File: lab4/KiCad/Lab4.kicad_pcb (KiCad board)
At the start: 2 copper layers, 120 x 234 mm, 287 parts, among them J1 Sense test points, J10 CAN A isolation, J11 CAN A test, J14 CAN B isolation, J15 CAN B test, J2 Current test, J20 CAN A isolation, J21 CAN A test, J24 CAN B isolation, J25 CAN B test, J3 Current test, J30 CAN A isolation, J31 CAN A test, J34 CAN B isolation, J35 CAN B test, J40 Battery input: 1=+ 2=GND, J41 VBAT test, J42 Rail / PG / GND, J43 Rail / PG / GND, J44 Rail / PG / GND, J500 BOOT recovery, J501 SWD (2.54mm), J502 3.3V TTL UART, J503 LAB3 rows 1-13, J504 Additional probes, J505 Reserved / encoder probes, J550 FRONT LEFT lamp, J551 FRONT RIGHT lamp, J600 BOOT recovery, J601 SWD (2.54mm), J602 3.3V TTL UART, J603 LAB3 rows 1-13, J604 Additional probes, J605 Reserved / encoder probes, J650 REAR LEFT lamp, J651 REAR RIGHT lamp, J70 Raspberry Pi4 GPIO, J703 LAB3 rows 1-13, J704 Pi extra probes, J80 LEFT motor, J81 RIGHT motor, J82 LEFT encoder, J83 RIGHT encoder, J90 Servo: GND / 6.6V / PWM, Q1 DMPH3010LK3-13, Q550 MMBT3904, Q551 MMBT3904, Q650 MMBT3904, Q651 MMBT3904, U1 INA180A2IDBVR, U10 MCP2515T-I/ST, U11 SN65HVD231DR, U14 MCP2515T-I/ST, U15 SN65HVD231DR, U2 ACS712ELCTR-05B-T, U20 MCP2515T-I/ST, U21 SN65HVD231DR, U24 MCP2515T-I/ST, U25 SN65HVD231DR, U3 ACS712ELCTR-05B-T, U30 MCP2515T-I/ST, U31 SN65HVD231DR, U34 MCP2515T-I/ST, U35 SN65HVD231DR, U40 TPS564252DRLR, U41 TPS564252DRLR, U42 TPS564252DRLR, U50 STM32F401RET6TR, U60 STM32F401RET6TR, U80 L298N, U81 SN74LVC14APWR, Y10 16 MHz, Y14 16 MHz, Y20 16 MHz, Y24 16 MHz, Y30 16 MHz, Y34 16 MHz

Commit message: Add verified GCT switch footprints and refresh Lab 4 checks
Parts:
- added SW50: SWT0210-045026GSA, Lab4_Switches:GCT_SWT0210_4.5x4.5mm, F.Cu at (52.0, 225.0)
- added SW51: SWT0210-045026GSA, Lab4_Switches:GCT_SWT0210_4.5x4.5mm, F.Cu at (100.0, 219.0)
- added SW60: SWT0210-045026GSA, Lab4_Switches:GCT_SWT0210_4.5x4.5mm, F.Cu at (52.0, 121.0)
- added SW61: SWT0210-045026GSA, Lab4_Switches:GCT_SWT0210_4.5x4.5mm, F.Cu at (67.0, 125.0)
- added SW70: SWT0210-045026GSA, Lab4_Switches:GCT_SWT0210_4.5x4.5mm, F.Cu at (52.0, 184.0)
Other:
- board text removed: "SW50 RESET"
- board text removed: "SW51 SELF TEST"
- board text removed: "SW60 RESET"
- board text removed: "SW61 SELF TEST"
- board text removed: "SW70 PI TEST"

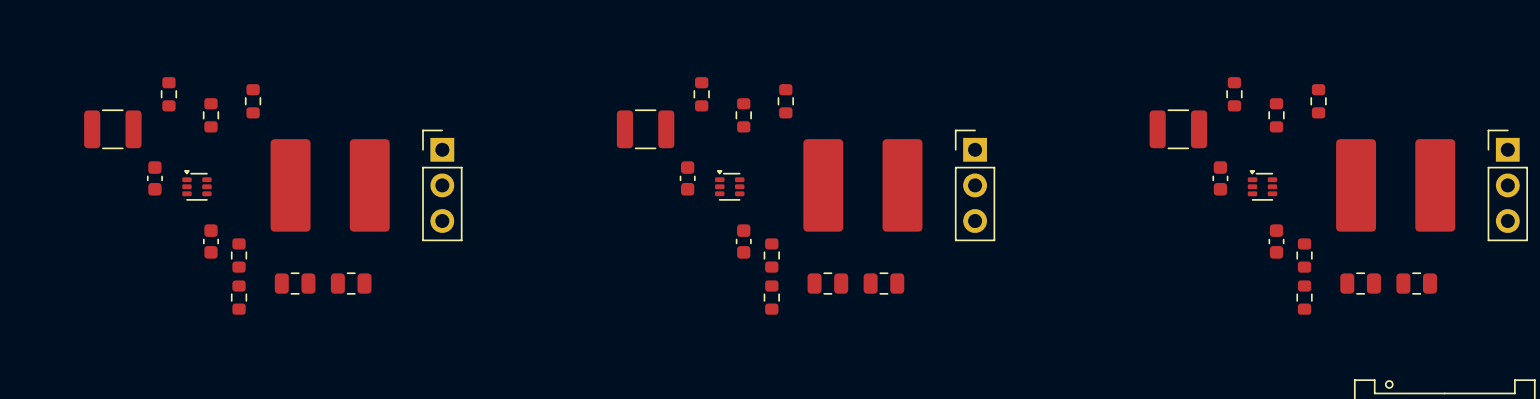
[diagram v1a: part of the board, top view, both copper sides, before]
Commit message: Refine regulator placement and verify buck support circuits
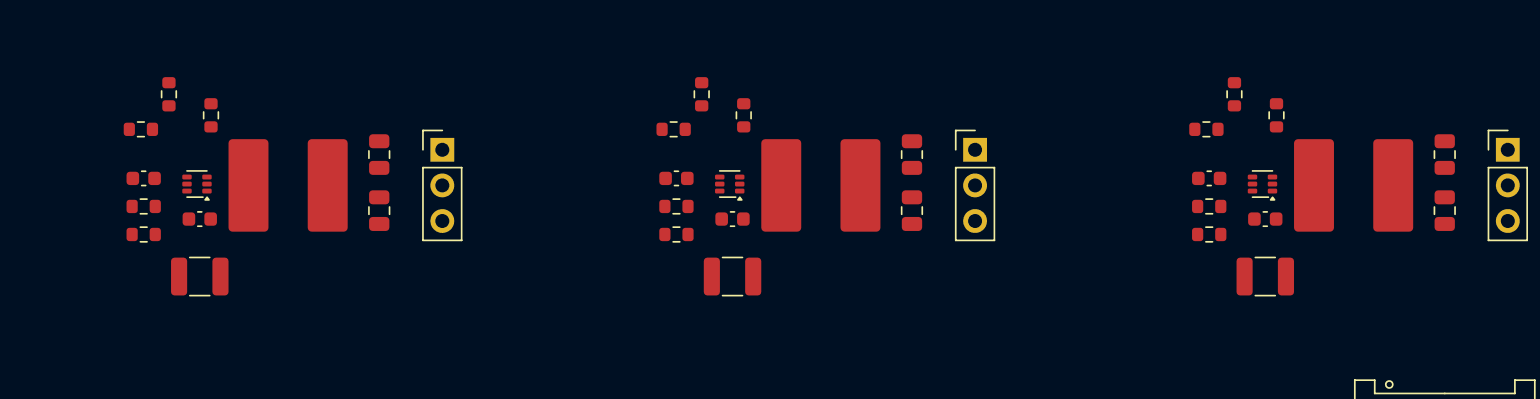
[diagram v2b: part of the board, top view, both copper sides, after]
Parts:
- moved C410 12.2 mm to (58.2, 250.5), turned to 180 degrees
- moved C420 12.2 mm to (96.2, 250.5), turned to 180 degrees
- moved C430 12.2 mm to (134.2, 250.5), turned to 180 degrees
- moved C412 11.0 mm to (71.0, 241.8), turned to 90 degrees
- moved C422 11.0 mm to (109.0, 241.8), turned to 90 degrees
- moved C432 11.0 mm to (147.0, 241.8), turned to 90 degrees
- moved R414 8.25 mm to (54.0, 240.0), turned to 0 degrees
- moved R424 8.25 mm to (92.0, 240.0), turned to 0 degrees
- moved R434 8.25 mm to (130.0, 240.0), turned to 0 degrees
- moved R431 8.15 mm to (130.2, 247.5), turned to 180 degrees
- moved R411 8.15 mm to (54.2, 247.5), turned to 180 degrees
- moved R421 8.15 mm to (92.2, 247.5), turned to 180 degrees
- moved R430 7.65 mm to (130.2, 245.5), turned to 0 degrees
- moved R410 7.65 mm to (54.2, 245.5), turned to 0 degrees
- moved R420 7.65 mm to (92.2, 245.5), turned to 0 degrees
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
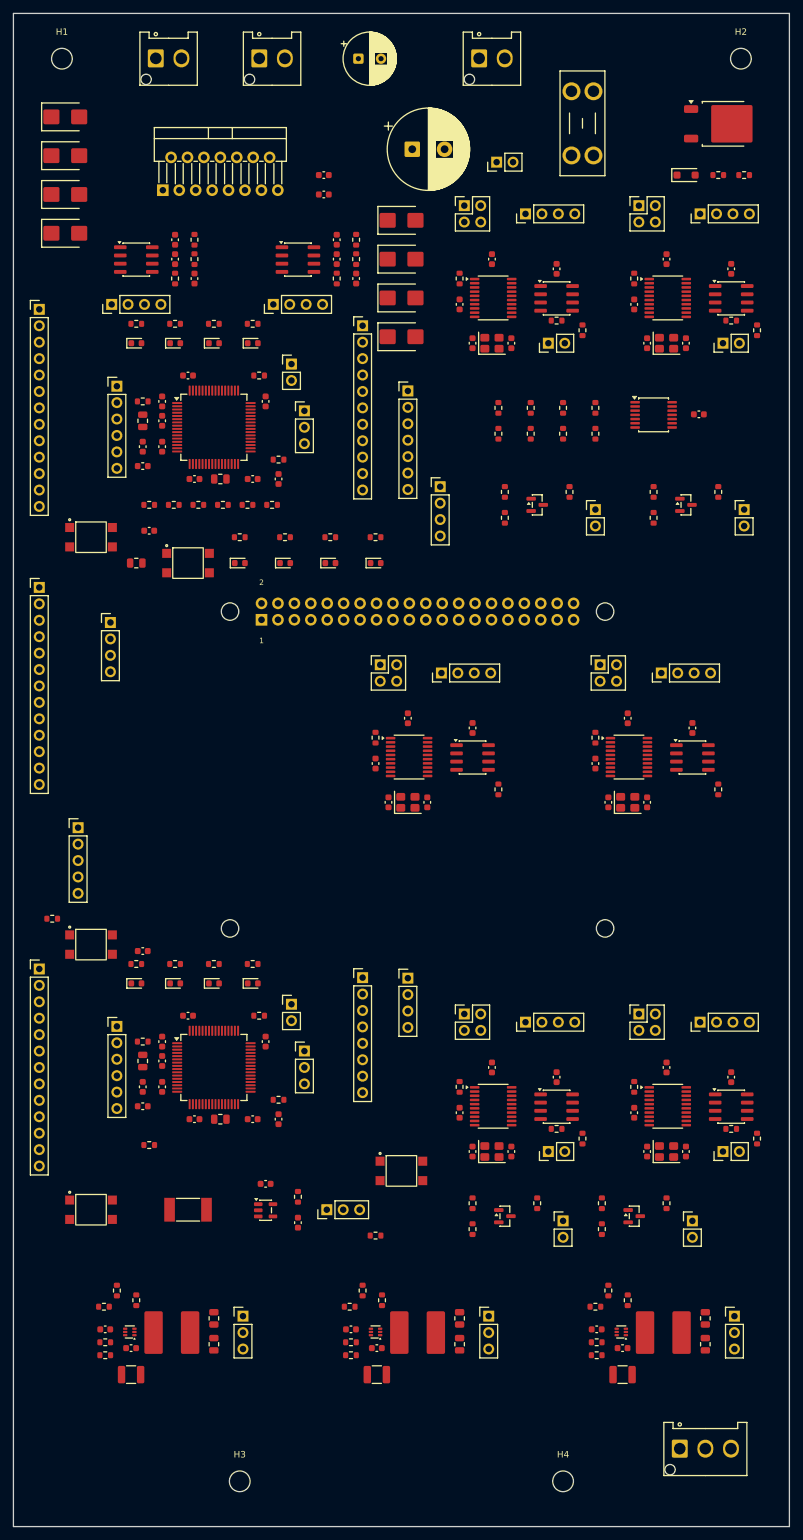
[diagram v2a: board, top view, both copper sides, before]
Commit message: Start regulator copper routing and verify local connectivity
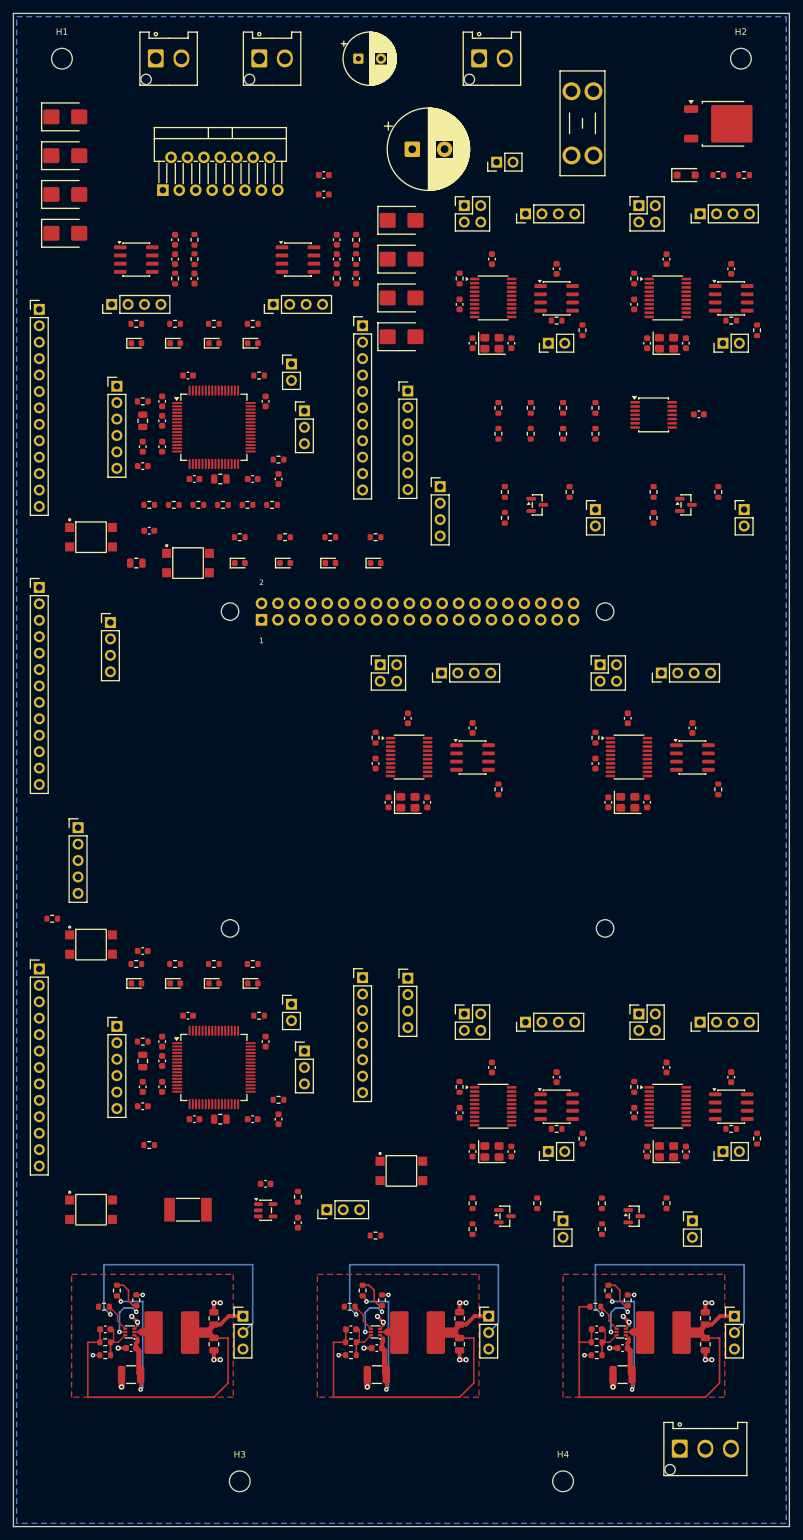
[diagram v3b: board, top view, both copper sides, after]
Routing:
- net /VBAT_PROTECTED: track 0.00 -> 81.7 mm, vias 0 -> 6
- net /+3V3: track 0.00 -> 61.9 mm
- net /+6V6_SERVO: track 0.00 -> 54.8 mm
- net /+5V: track 0.00 -> 54.8 mm
- net /Power/P_3V3_PG: track 0.00 -> 47.9 mm, vias 0 -> 1
- net /Power/P_SERVO_PG: track 0.00 -> 47.9 mm, vias 0 -> 1
- net /Power/P_5V_PG: track 0.00 -> 47.9 mm, vias 0 -> 1
- net /GND: track 0.00 -> 37.7 mm, vias 0 -> 30
- net /Power/P_SERVO_EN: track 0.00 -> 13.3 mm, vias 0 -> 2
- net /Power/P_5V_EN: track 0.00 -> 13.3 mm, vias 0 -> 2
- net /Power/P_3V3_EN: track 0.00 -> 13.3 mm, vias 0 -> 2
- net /Power/P_SERVO_FB: track 0.00 -> 7.72 mm
- net /Power/P_5V_FB: track 0.00 -> 7.72 mm
- net /Power/P_3V3_FB: track 0.00 -> 7.72 mm
- net /Power/P_3V3_SW: track 0.00 -> 2.97 mm
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- added copper zone on B.Cu, net /GND
- added copper zone on F.Cu, net /GND

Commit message: Route MCU and CAN local support circuits
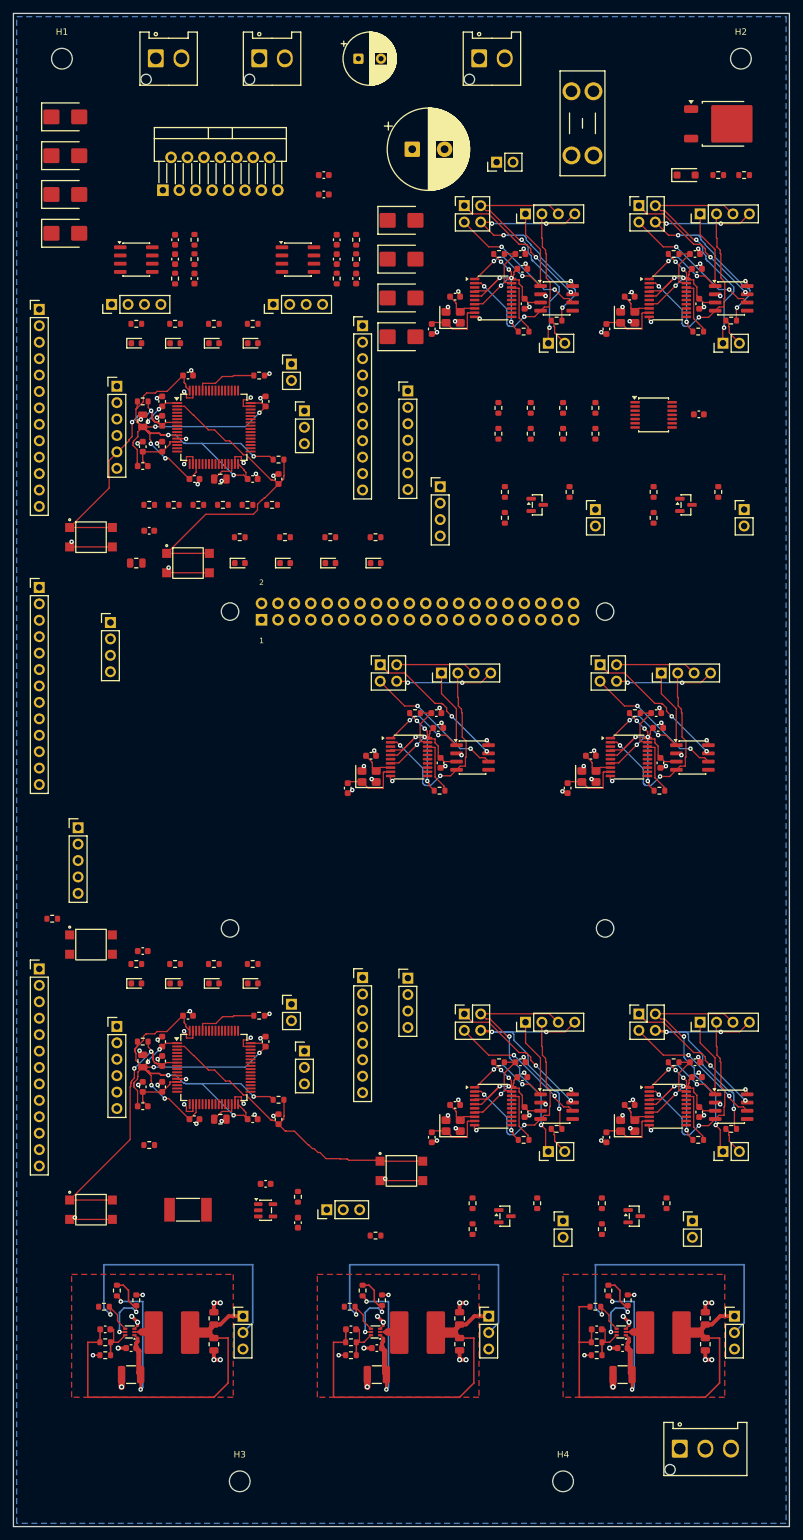
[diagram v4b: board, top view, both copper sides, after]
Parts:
- moved C202 12.2 mm to (118.4, 77.2), turned to 0 degrees
- moved C242 12.2 mm to (145.4, 77.2), turned to 0 degrees
- moved C102 12.2 mm to (118.4, 202.2), turned to 0 degrees
- moved C142 12.2 mm to (145.4, 202.2), turned to 0 degrees
- moved C302 12.2 mm to (105.4, 148.2), turned to 0 degrees
- moved C342 12.2 mm to (139.4, 148.2), turned to 0 degrees
- moved C201 11.3 mm to (108.3, 83.8), turned to 0 degrees
- moved C101 11.3 mm to (108.3, 208.8), turned to 0 degrees
- moved C301 11.3 mm to (95.3, 154.8), turned to 0 degrees
- moved C241 11.3 mm to (135.3, 83.8), turned to 0 degrees
- moved C141 11.3 mm to (135.3, 208.8), turned to 0 degrees
- moved C341 11.3 mm to (129.3, 154.8), turned to 0 degrees
- moved R101 9.10 mm to (118.9, 214.2), turned to 0 degrees
- moved R141 9.10 mm to (145.9, 214.2), turned to 0 degrees
- moved R301 9.10 mm to (105.9, 160.2), turned to 0 degrees
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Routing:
- net /+3V3: track 61.9 -> 540.5 mm, vias 0 -> 54
- net /GND: track 37.7 -> 176.8 mm, vias 30 -> 128
- net /CAN_B_L: track 0.00 -> 94.4 mm, vias 0 -> 9
- net /CAN_A_L: track 0.00 -> 94.4 mm, vias 0 -> 9
- net /CAN_B_H: track 0.00 -> 91.7 mm, vias 0 -> 4
- net /CAN_A_H: track 0.00 -> 91.7 mm, vias 0 -> 4
- net /Rear zone/R_SELFTEST_BUTTON: track 0.00 -> 53.8 mm
- net /Front zone/F_SELFTEST_BUTTON: track 0.00 -> 49.6 mm
- net /Front zone/F_RESET_N: track 0.00 -> 45.2 mm, vias 0 -> 2
- net /Rear zone/R_RESET_N: track 0.00 -> 41.6 mm, vias 0 -> 2
- net /Cockpit zone/PI_A_RXD: track 0.00 -> 32.1 mm, vias 0 -> 2
- net /Front zone/F_A_RXD: track 0.00 -> 32.1 mm, vias 0 -> 2
- net /Rear zone/R_A_RXD: track 0.00 -> 32.1 mm, vias 0 -> 2
- net /Front zone/F_B_RXD: track 0.00 -> 32.0 mm, vias 0 -> 2
- net /Rear zone/R_B_RXD: track 0.00 -> 32.0 mm, vias 0 -> 2
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
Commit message: Route CAN A and B backbones across all three zones
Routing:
- net /CAN_A_H: track 91.7 -> 256.6 mm
- net /CAN_A_L: track 94.4 -> 251.3 mm, vias 9 -> 13
- net /CAN_B_H: track 91.7 -> 242.0 mm
- net /CAN_B_L: track 94.4 -> 236.8 mm, vias 9 -> 13

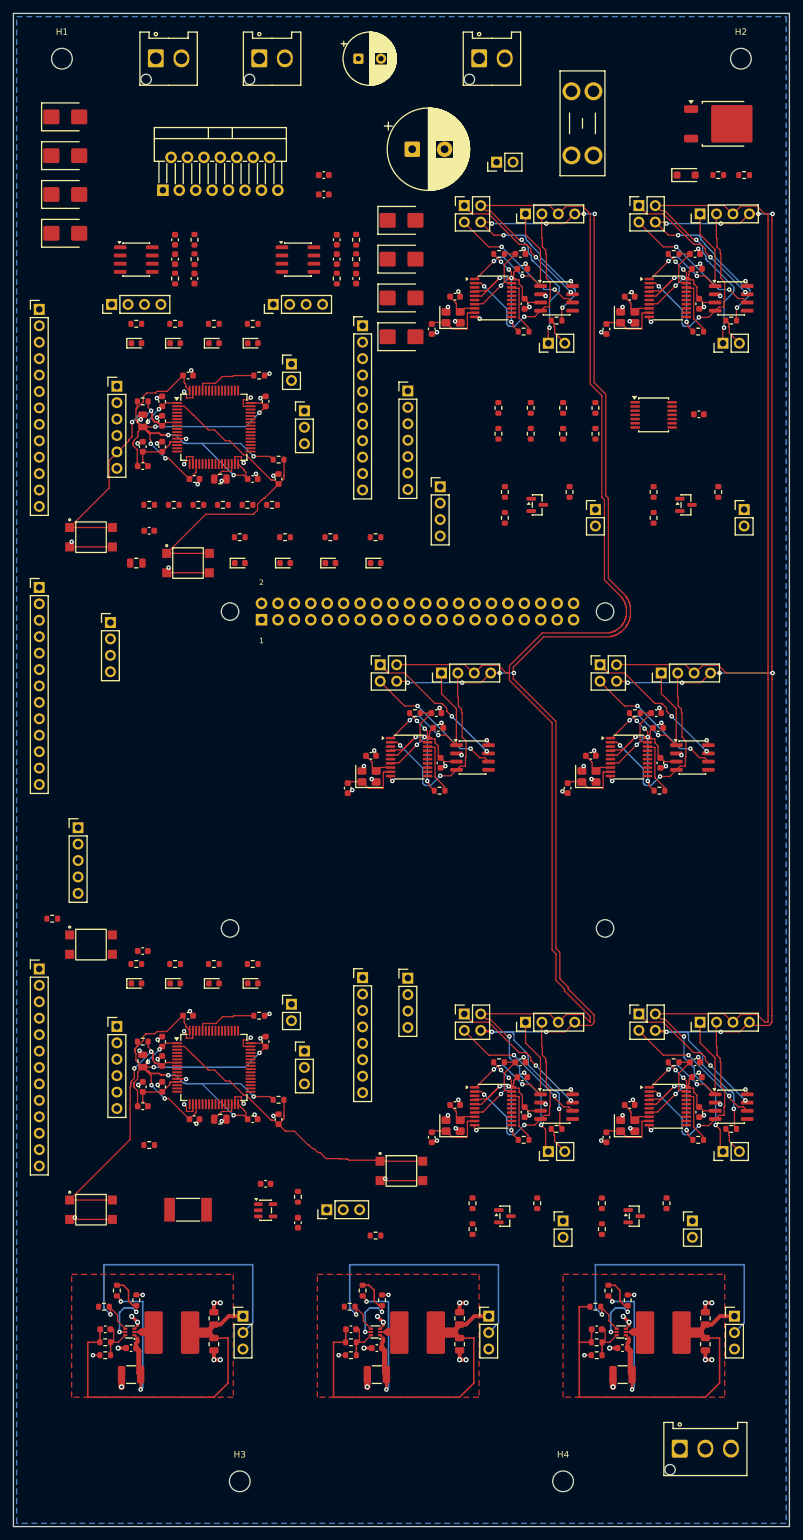
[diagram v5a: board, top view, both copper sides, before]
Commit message: Route Lab 4 host interfaces and repair affected ground connections
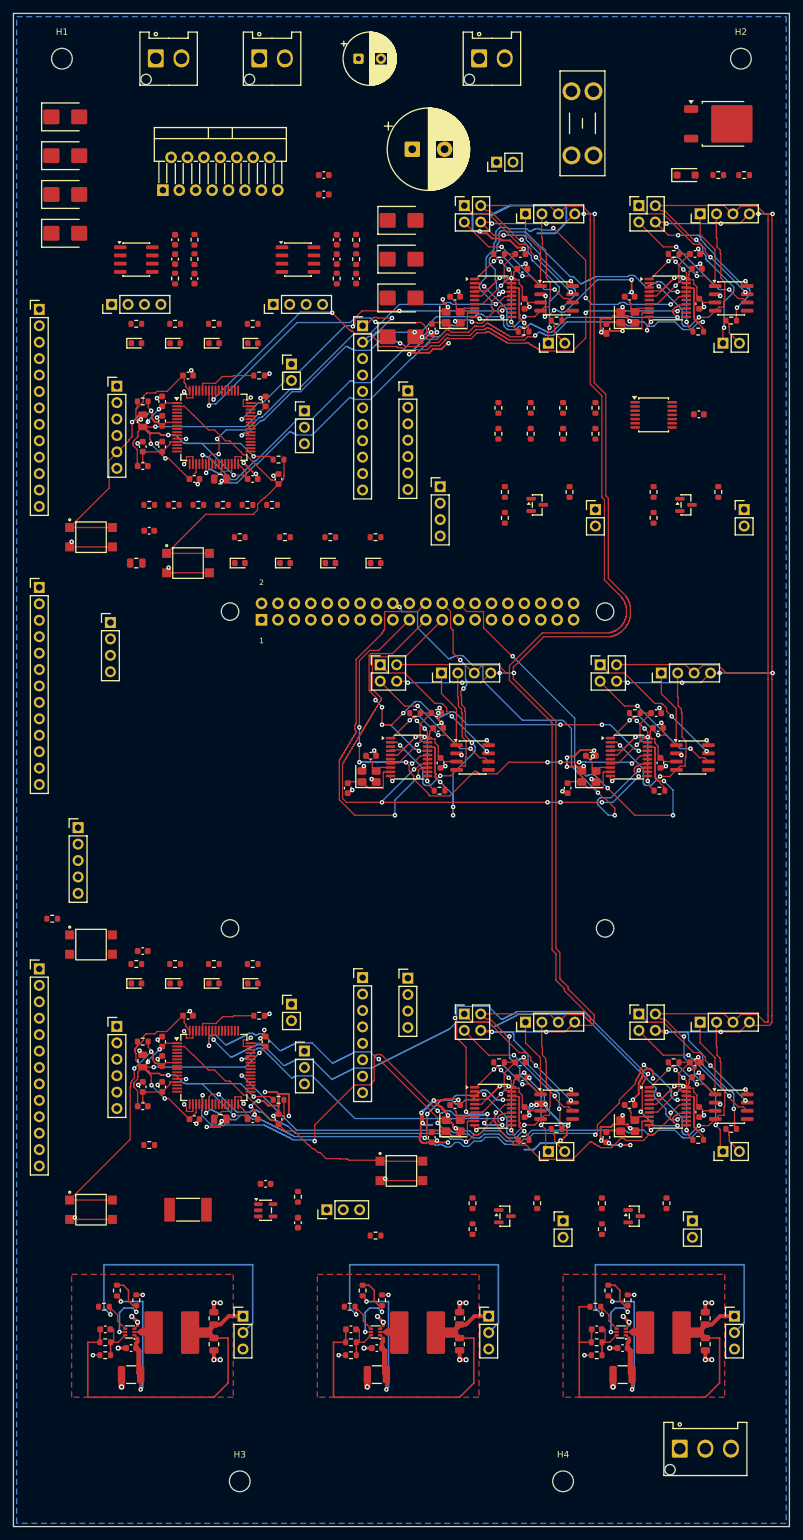
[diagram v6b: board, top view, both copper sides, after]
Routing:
- net /GND: track 176.8 -> 408.4 mm, vias 128 -> 165
- net /Front zone/F_SCK: track 0.00 -> 149.6 mm, vias 0 -> 11
- net /Front zone/F_MISO: track 0.00 -> 128.3 mm, vias 0 -> 7
- net /Rear zone/R_MOSI: track 0.00 -> 113.5 mm, vias 0 -> 6
- net /Rear zone/R_MISO: track 0.00 -> 110.6 mm, vias 0 -> 5
- net /Cockpit zone/PI_SCK: track 0.00 -> 99.5 mm, vias 0 -> 6
- net /Rear zone/R_SCK: track 0.00 -> 99.2 mm, vias 0 -> 3
- net /Front zone/F_MOSI: track 0.00 -> 93.7 mm, vias 0 -> 4
- net /Rear zone/R_CS_B: track 8.54 -> 102.1 mm, vias 0 -> 4
- net /Front zone/F_INT_B: track 0.00 -> 93.1 mm, vias 0 -> 2
- net /Rear zone/R_INT_B: track 0.00 -> 91.0 mm, vias 0 -> 4
- net /Cockpit zone/PI_MOSI: track 0.00 -> 88.3 mm, vias 0 -> 9
- net /Front zone/F_CS_B: track 8.54 -> 96.3 mm, vias 0 -> 2
- net /Cockpit zone/PI_MISO: track 0.00 -> 78.0 mm, vias 0 -> 8
- net /Front zone/F_CS_A: track 8.64 -> 80.7 mm, vias 0 -> 4
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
